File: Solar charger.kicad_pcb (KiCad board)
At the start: 2 copper layers, 73.5 x 39.7 mm, 12 parts, among them J1 SOLAR_IN, J2 BATTERY, J3 POWER_OUT, J4 BAT_MON, U1 MCP1700x-330xxTO, U2 TP4056

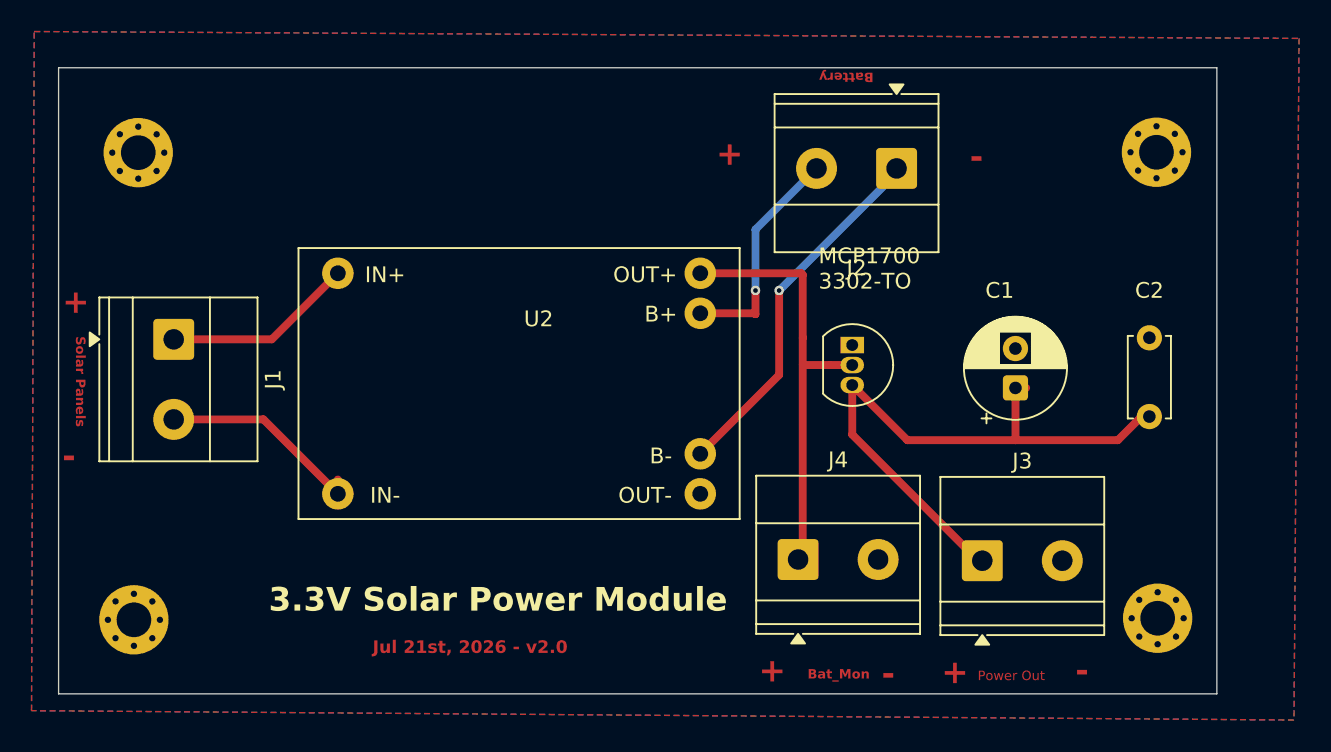
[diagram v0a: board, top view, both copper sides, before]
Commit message: Fix TP4056 pads spacing, replace volatge regulator, tweaks (#5)
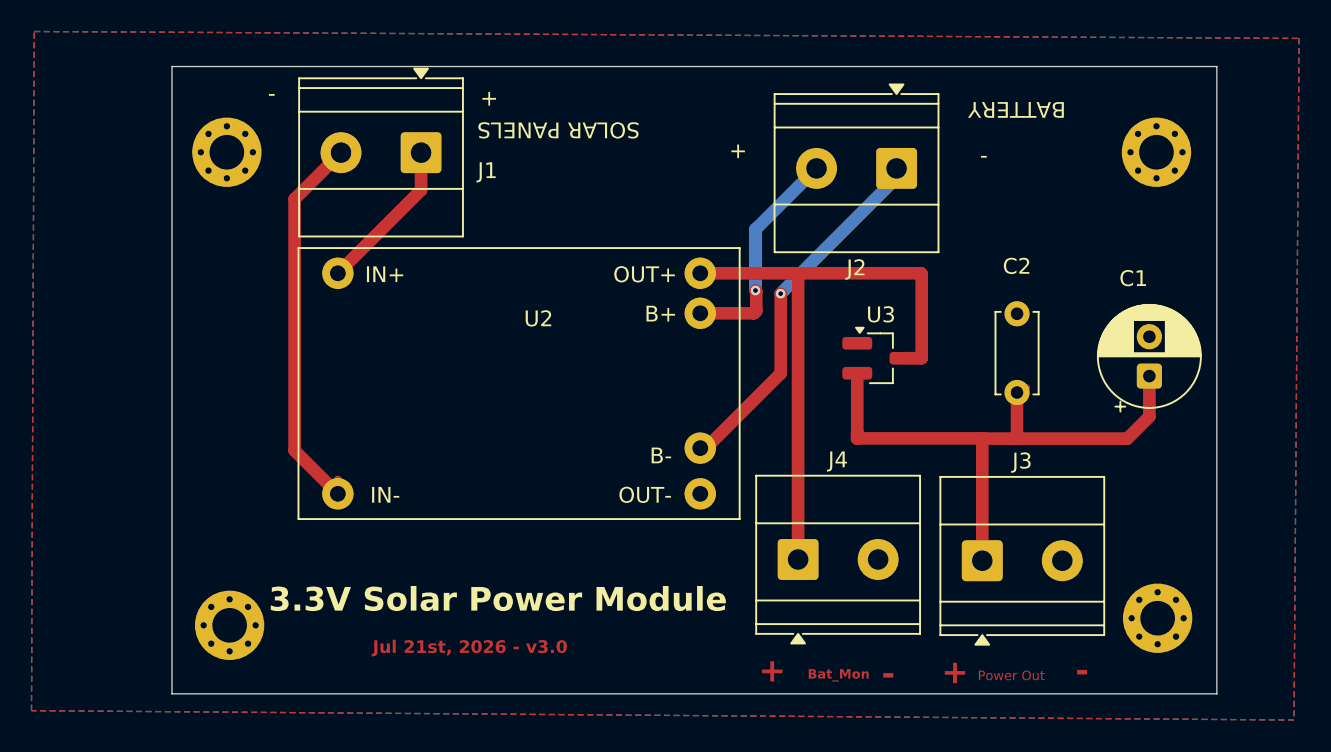
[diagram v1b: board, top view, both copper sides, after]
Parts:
- removed U1: MCP1700x-330xxTO, Package_TO_SOT_THT:TO-92_Inline
- added U3: MCP1700x-330xxTT, Package_TO_SOT_SMD:SOT-23_Handsoldering, F.Cu at (204.5, 87.8)
- moved J1 19.7 mm to (175.3, 74.8), turned to 180 degrees
- moved C2 8.54 mm to (213.1, 85.0)
- moved C1 8.53 mm to (221.5, 88.9)
- moved H2 6.09 mm to (163.1, 104.8)
- moved H1 5.63 mm to (162.9, 74.7)
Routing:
- net /SOLAR_GND: track 13.3 -> 24.9 mm
- net /BAT_OUT: track 27.9 -> 39.1 mm
- net /SOLAR_IN: track 12.2 -> 9.84 mm
- net /3V3 OUT: track 39.6 -> 38.5 mm
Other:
- board size 73.5 x 39.7 mm -> 66.3 x 39.8 mm
- board text added: "BATTERY"
- board text added: "Jul 21st, 2026 - v3.0"
- board text added: "SOLAR PANELS"
- board text removed: "Battery"
- board text removed: "Jul 21st, 2026 - v2.0"
- board text removed: "MCP1700 3302-TO"
- board text removed: "Solar Panels"
